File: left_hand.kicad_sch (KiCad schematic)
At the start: 1 part

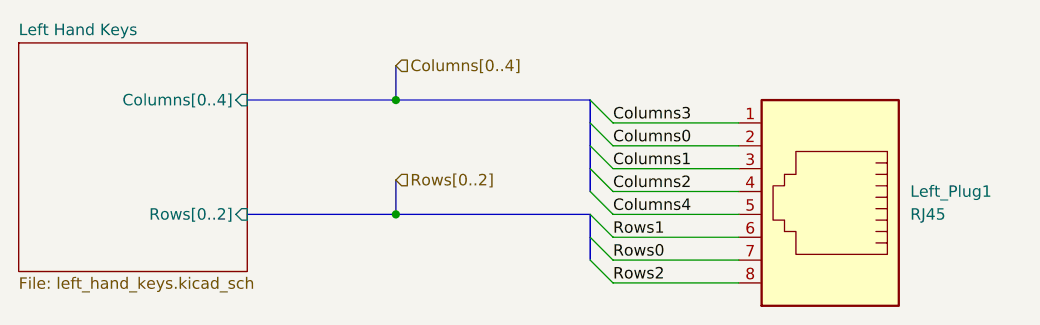
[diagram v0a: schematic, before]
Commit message: Match left hand pins
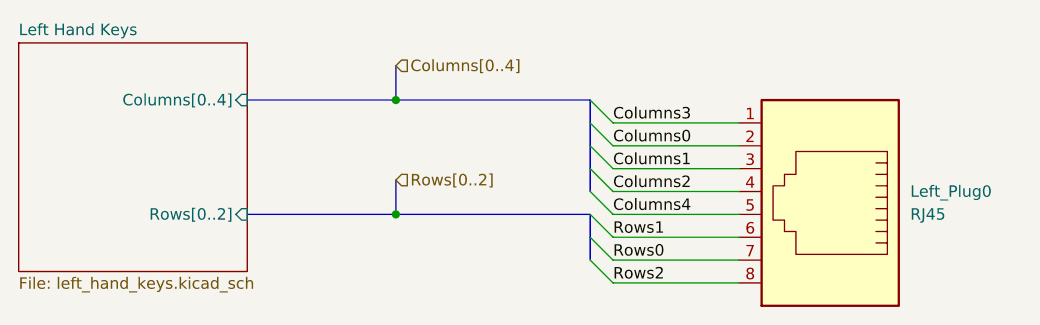
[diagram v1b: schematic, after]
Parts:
- renumbered Left_Plug1 to Left_Plug0
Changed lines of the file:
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@@
 		(dnp no)
 		(fields_autoplaced yes)
-		(property "Reference" "Left_Plug1"
+		(property "Reference" "Left_Plug0"
 			(at 157.48 64.7699 0)
 			(effects

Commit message: Rework right hand
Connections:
- net Columns0: now also Left_Plug0.4; no longer Left_Plug0.2
- net Columns2: now also Left_Plug0.2; no longer Left_Plug0.4
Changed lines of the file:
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@@
 		)
 	)
-	(label "Columns0"
+	(label "Columns2"
 		(at 124.46 59.69 0)
 		(effects
@@
 		)
 	)
-	(label "Columns2"
+	(label "Columns0"
 		(at 124.46 64.77 0)
 		(effects
